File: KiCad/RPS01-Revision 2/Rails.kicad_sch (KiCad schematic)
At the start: 45 parts, among them U11 LM340MPX-5.0/NOPB, U21 LM340MPX-5.0/NOPB

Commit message: updates
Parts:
- C? (x4), C_FF? (x2): value 0.1u DNI -> 0.1u
- C_FF? (x2): value 0.22u DNI -> 0.22u
- C_FF?: value 22u DNI -> 22u
- C_FF?: value 3.65n DNI -> 3.65n
- C_FF?: value 0.47u DNI -> 0.47u
- C_IN? (x2): value 100u DNI -> 100u
- C_OUT? (x2): value 220u DNI -> 220u
- L?: value 53u DNI -> 53u
- L?: value 37u DNI -> 37u
- R? (x2): value 1k DNI -> 1k
- R?: value 8.87k DNI -> 8.87k
- R?: value 3.16k DNI -> 3.16k
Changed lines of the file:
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@@
       (effects (font (size 1.27 1.27)) (justify left))
     )
-    (property "Value" "0.1u DNI" (at 114.3508 271.2212 0)
+    (property "Value" "0.1u" (at 114.3508 271.2212 0)
       (effects (font (size 1.27 1.27)) (justify left))
     )
@@
       (effects (font (size 1.27 1.27)) (justify right))
     )
-    (property "Value" "0.22u DNI" (at 89.963 104.3448 90)
+    (property "Value" "0.22u" (at 89.963 104.3448 90)
       (effects (font (size 1.27 1.27)) (justify right))
     )
@@
   (symbol (lib_id "Device:C_Polarized") (at 341.63 120.396 0) (unit 1)
     (in_bom yes) (on_board yes) (dnp no) (fields_autoplaced)
-    (property "Reference" "C_OUT?" (at 345.44 118.237 0)
-      (effects (font (size 1.27 1.27)) (justify left))
-    )
-    (property "Value" "220u DNI" (at 345.44 120.777 0)
+    (property "Reference" "C_OUT?" (at 345.44 118.872 0)
+      (effects (font (size 1.27 1.27)) (justify left))
+    )
+    (property "Value" "220u" (at 345.44 121.412 0)
       (effects (font (size 1.27 1.27)) (justify left))
     )
@@
   (symbol (lib_id "Device:C_Polarized") (at 513.08 121.92 0) (unit 1)
     (in_bom yes) (on_board yes) (dnp no) (fields_autoplaced)
-    (property "Reference" "C_OUT?" (at 516.89 119.761 0)
-      (effects (font (size 1.27 1.27)) (justify left))
-    )
-    (property "Value" "220u DNI" (at 516.89 122.301 0)
+    (property "Reference" "C_OUT?" (at 516.89 120.396 0)
+      (effects (font (size 1.27 1.27)) (justify left))
+    )
+    (property "Value" "220u" (at 516.89 122.936 0)
       (effects (font (size 1.27 1.27)) (justify left))
     )
@@
       (effects (font (size 1.27 1.27)))
     )
-    (property "Value" "53u DNI" (at 329.1552 108.8207 90)
+    (property "Value" "53u" (at 329.1552 108.8207 90)
       (effects (font (size 1.27 1.27)))
     )
@@
       (effects (font (size 1.27 1.27)) (justify right))
     )
-    (property "Value" "22u DNI" (at 91.44 35.56 90)
+    (property "Value" "22u" (at 91.44 35.56 90)
       (effects (font (size 1.27 1.27)) (justify right))
     )
@@
       (effects (font (size 1.27 1.27)) (justify left))
     )
-    (property "Value" "0.1u DNI" (at 115.57 224.79 0)
+    (property "Value" "0.1u" (at 115.57 224.79 0)
       (effects (font (size 1.27 1.27)) (justify left))
     )
@@
   (symbol (lib_id "Device:C_Small") (at 130.302 210.058 0) (unit 1)
     (in_bom yes) (on_board yes) (dnp no) (fields_autoplaced)
-    (property "Reference" "C?" (at 133.35 208.7943 0)
-      (effects (font (size 1.27 1.27)) (justify left))
-    )
-    (property "Value" "0.1u DNI" (at 133.35 211.3343 0)
+    (property "Reference" "C?" (at 133.35 209.4293 0)
+      (effects (font (size 1.27 1.27)) (justify left))
+    )
+    (property "Value" "0.1u" (at 133.35 211.9693 0)
       (effects (font (size 1.27 1.27)) (justify left))
     )
@@
       (effects (font (size 1.27 1.27)) (justify right))
     )
-    (property "Value" "3.65n DNI" (at 502.92 76.2 90)
+    (property "Value" "3.65n" (at 502.92 76.2 90)
       (effects (font (size 1.27 1.27)) (justify right))
     )
@@
   (symbol (lib_id "Device:C_Small") (at 130.302 255.778 0) (unit 1)
     (in_bom yes) (on_board yes) (dnp no) (fields_autoplaced)
-    (property "Reference" "C?" (at 133.35 254.5143 0)
-      (effects (font (size 1.27 1.27)) (justify left))
-    )
-    (property "Value" "0.1u DNI" (at 133.35 257.0543 0)
+    (property "Reference" "C?" (at 133.35 255.1493 0)
+      (effects (font (size 1.27 1.27)) (justify left))
+    )
+    (property "Value" "0.1u" (at 133.35 257.6893 0)
       (effects (font (size 1.27 1.27)) (justify left))
     )
@@
       (effects (font (size 1.27 1.27)) (justify right))
     )
-    (property "Value" "0.47u DNI" (at 91.1688 53.3982 90)
+    (property "Value" "0.47u" (at 91.1688 53.3982 90)
       (effects (font (size 1.27 1.27)) (justify right))
     )
@@
       (effects (font (size 1.27 1.27)) (justify right))
     )
-    (property "Value" "0.22u DNI" (at 88.2127 136.3649 90)
+    (property "Value" "0.22u" (at 88.2127 136.3649 90)
       (effects (font (size 1.27 1.27)) (justify right))
     )
@@
   (symbol (lib_id "Device:C_Polarized") (at 266.7 118.11 0) (unit 1)
     (in_bom yes) (on_board yes) (dnp no) (fields_autoplaced)
-    (property "Reference" "C_IN?" (at 270.51 115.951 0)
-      (effects (font (size 1.27 1.27)) (justify left))
-    )
-    (property "Value" "100u DNI" (at 270.51 118.491 0)
+    (property "Reference" "C_IN?" (at 270.51 116.586 0)
+      (effects (font (size 1.27 1.27)) (justify left))
+    )
+    (property "Value" "100u" (at 270.51 119.126 0)
       (effects (font (size 1.27 1.27)) (justify left))
     )
@@
       (effects (font (size 1.27 1.27)) (justify right))
     )
-    (property "Value" "1k DNI" (at 307.34 88.9 90)
+    (property "Value" "1k" (at 307.34 88.9 90)
       (effects (font (size 1.27 1.27)) (justify right))
     )
@@
       (effects (font (size 1.27 1.27)) (justify right))
     )
-    (property "Value" "8.87k DNI\n" (at 500.38 90.17 90)
+    (property "Value" "8.87k\n" (at 500.38 90.17 90)
       (effects (font (size 1.27 1.27)) (justify right))
     )
@@
       (effects (font (size 1.27 1.27)) (justify right))
     )
-    (property "Value" "1k DNI" (at 481.33 90.17 90)
+    (property "Value" "1k" (at 481.33 90.17 90)
       (effects (font (size 1.27 1.27)) (justify right))
     )
@@
       (effects (font (size 1.27 1.27)) (justify right))
     )
-    (property "Value" "3.16k DNI" (at 328.93 88.9 90)
+    (property "Value" "3.16k" (at 328.93 88.9 90)
       (effects (font (size 1.27 1.27)) (justify right))
     )
@@
       (effects (font (size 1.27 1.27)) (justify right))
     )
-    (property "Value" "0.1u DNI" (at 130.5444 135.6786 90)
+    (property "Value" "0.1u" (at 130.5444 135.6786 90)
       (effects (font (size 1.27 1.27)) (justify right))
     )
@@
   (symbol (lib_id "Device:C_Polarized") (at 438.15 119.38 0) (unit 1)
     (in_bom yes) (on_board yes) (dnp no) (fields_autoplaced)
-    (property "Reference" "C_IN?" (at 441.96 117.221 0)
-      (effects (font (size 1.27 1.27)) (justify left))
-    )
-    (property "Value" "100u DNI" (at 441.96 119.761 0)
+    (property "Reference" "C_IN?" (at 441.96 117.856 0)
+      (effects (font (size 1.27 1.27)) (justify left))
+    )
+    (property "Value" "100u" (at 441.96 120.396 0)
       (effects (font (size 1.27 1.27)) (justify left))
     )
@@
   (symbol (lib_id "Device:L") (at 500.38 111.76 90) (unit 1)
     (in_bom yes) (on_board yes) (dnp no) (fields_autoplaced)
-    (property "Reference" "L?" (at 500.38 106.68 90)
-      (effects (font (size 1.27 1.27)))
-    )
-    (property "Value" "37u DNI" (at 500.38 109.22 90)
+    (property "Reference" "L?" (at 500.38 107.95 90)
+      (effects (font (size 1.27 1.27)))
+    )
+    (property "Value" "37u" (at 500.38 110.49 90)
       (effects (font (size 1.27 1.27)))
     )
@@
       (effects (font (size 1.27 1.27)) (justify right))
     )
-    (property "Value" "0.1u DNI" (at 131.6717 105.1986 90)
-      (effects (font (size 1.27 1.27)) (justify right))
-    )
+    (property "Value" "0.1u" (at 131.6717 105.1986 90)
+      (effects (font (size 1.27 1.27)) (justify right))
+    )

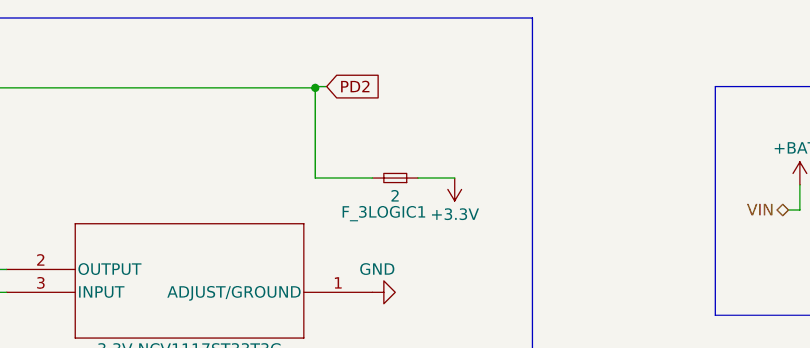
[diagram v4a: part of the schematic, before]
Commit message: Add Jumper for 3.3V Logic
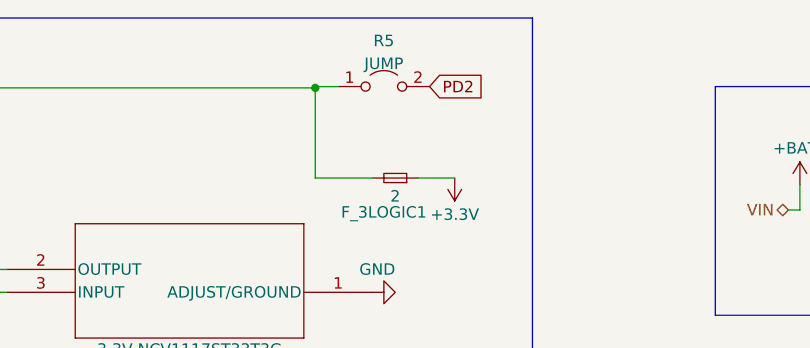
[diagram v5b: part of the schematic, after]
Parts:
- added R5: JUMP, Jumper:SolderJumper-2_P1.3mm_Open_TrianglePad1.0x1.5mm, symbol Jumper:Jumper_2_Open
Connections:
- net PD2: now also R5.2 (B); no longer C_FF?.1, F_3LOGIC1.2
- new net: C_FF?.1, F_3LOGIC1.2, R5.1 (A)
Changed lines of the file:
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@@
+    (stroke (width 0) (type default))
+  )
+  (wire (pts (xy 134.62 26.8134) (xy 134.62 36.83))
     (stroke (width 0) (type default))
   )
@@
     (stroke (width 0) (type default))
   )
+  (wire (pts (xy 134.62 26.67) (xy 137.16 26.67))
+    (stroke (width 0) (type default))
+  )
   (wire (pts (xy 466.09 130.81) (xy 485.14 130.81))
     (stroke (width 0.5) (type default))
@@
     (stroke (width 0) (type default))
   )
-  (wire (pts (xy 135.89 26.67) (xy 134.62 26.67))
-    (stroke (width 0) (type default))
-  )
   (wire (pts (xy 513.08 81.28) (xy 508 81.28))
     (stroke (width 0) (type default))
@@
     (stroke (width 0) (type default))
   )
-  (wire (pts (xy 134.62 26.8134) (xy 134.62 36.83))
-    (stroke (width 0) (type default))
-  )
   (wire (pts (xy 97.79 49.53) (xy 100.33 49.53))
     (stroke (width 0) (type default))
@@
     (stroke (width 0) (type default))
   )
-  (wire (pts (xy 134.62 26.8134) (xy 134.62 26.67))
+  (wire (pts (xy 134.62 26.67) (xy 134.62 26.8134))
     (stroke (width 0) (type default))
   )
@@
     )
   )
-  (global_label "PD2" (shape input) (at 135.89 26.67 0) (fields_autoplaced)
+  (global_label "PD2" (shape input) (at 147.32 26.67 0) (fields_autoplaced)
     (effects (font (size 1.27 1.27)) (justify left))
-    (property "Intersheetrefs" "${INTERSHEET_REFS}" (at 142.5453 26.67 0)
+    (property "Intersheetrefs" "${INTERSHEET_REFS}" (at 153.9753 26.67 0)
       (effects (font (size 1.27 1.27)) (justify left) hide)
     )
@@
         )
       )
+    )
+  )
+  (symbol (lib_id "Jumper:Jumper_2_Open") (at 142.24 26.67 0) (unit 1)
+    (in_bom yes) (on_board yes) (dnp no) (fields_autoplaced)
+    (property "Reference" "R5" (at 142.24 21.59 0)
+      (effects (font (size 1.27 1.27)))
+    )
+    (property "Value" "JUMP" (at 142.24 24.13 0)
+      (effects (font (size 1.27 1.27)))
+    )
+    (property "Footprint" "Jumper:SolderJumper-2_P1.3mm_Open_TrianglePad1.0x1.5mm" (at 142.24 26.67 0)
+      (effects (font (size 1.27 1.27)) hide)
+    )
+    (property "Datasheet" "~" (at 142.24 26.67 0)
+      (effects (font (size 1.27 1.27)) hide)
+    )
+    (pin "1")
+    (pin "2")
+    (instances
+      (project "rps01"
+        (path "/14930f15-c0a0-4b55-93e6-b112548415f6/6ed54b0f-f89c-4a82-b1ab-c92c0c126d05"
+          (reference "R5") (unit 1)
+        )
+      )

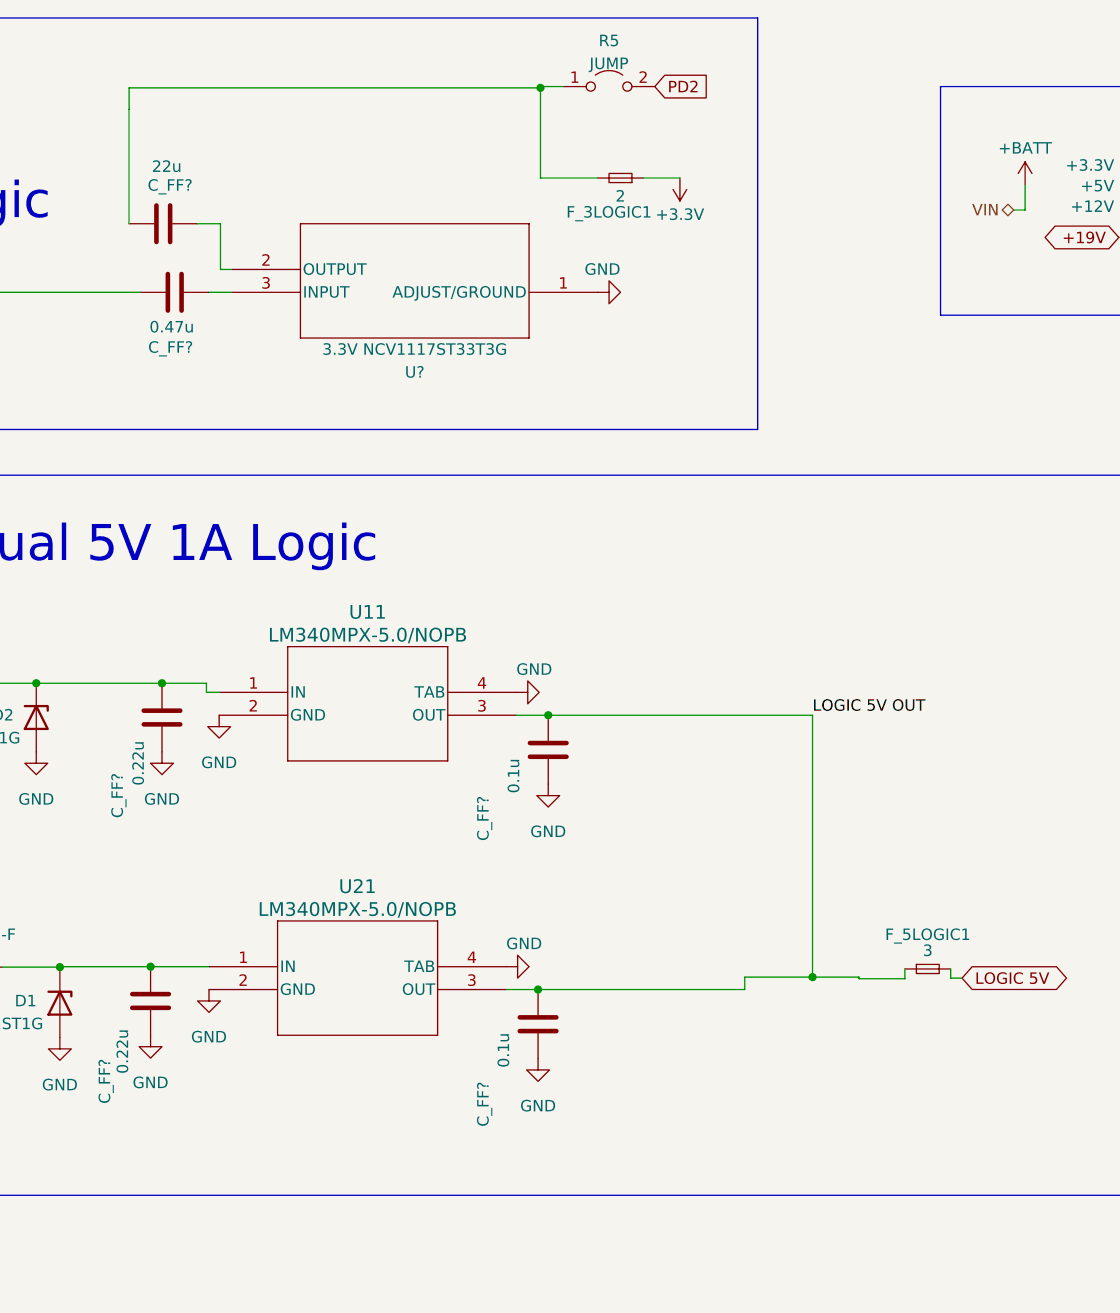
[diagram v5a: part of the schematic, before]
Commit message: Deleted one of the caps
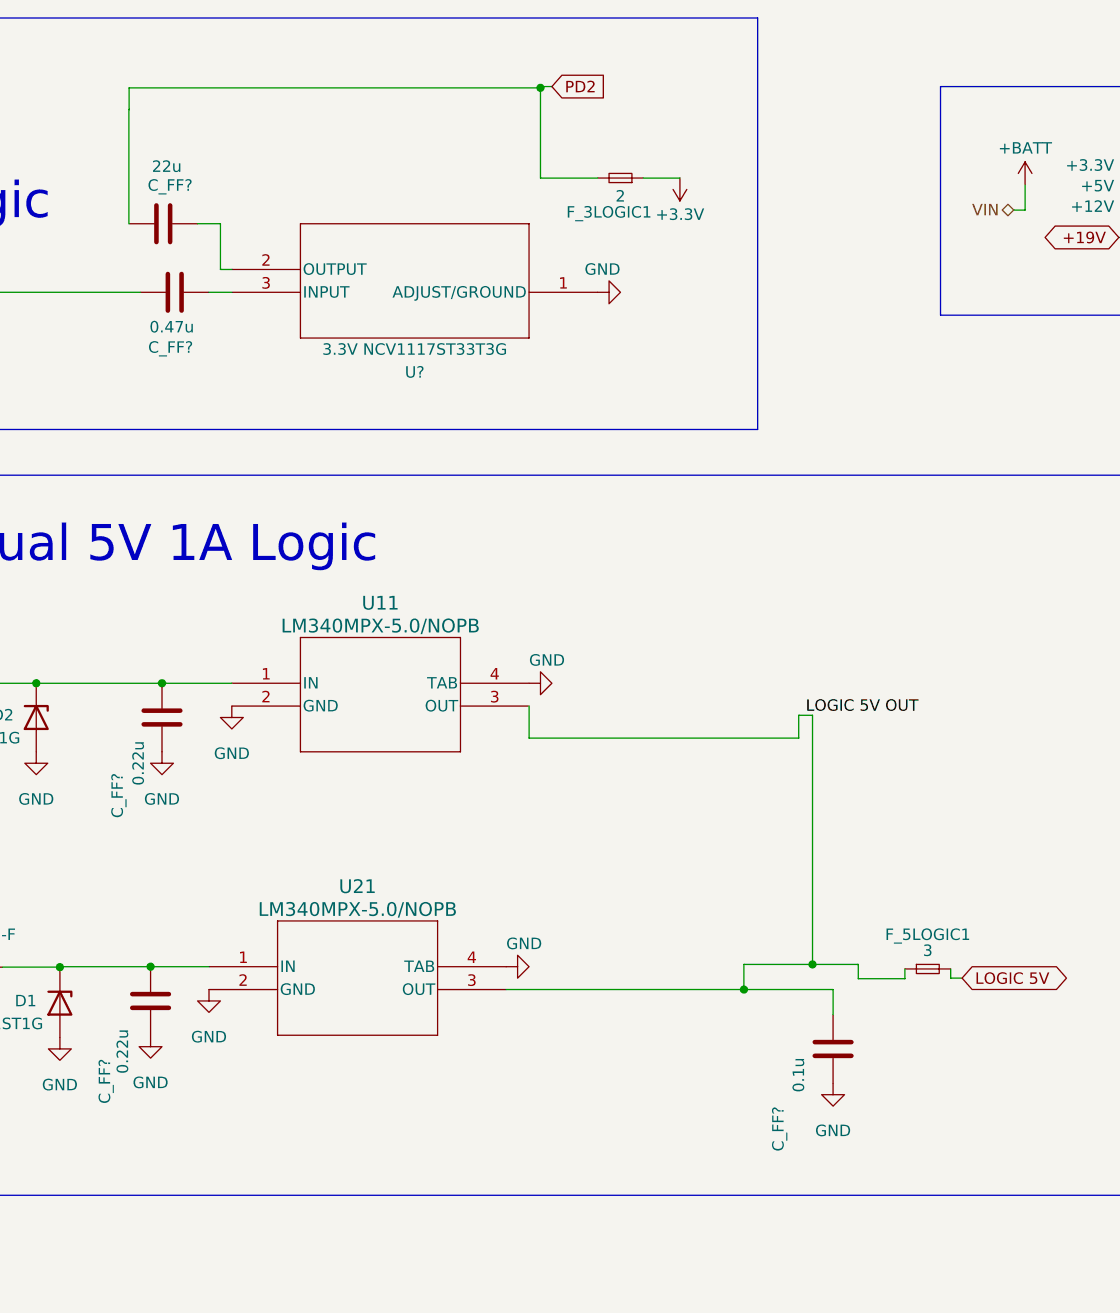
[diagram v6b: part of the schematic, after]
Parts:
- removed C_FF?: 0.1u, Capacitor_SMD:C_0603_1608Metric, symbol Device:C
- removed R5: JUMP, Jumper:SolderJumper-2_P1.3mm_Open_TrianglePad1.0x1.5mm, symbol Jumper:Jumper_2_Open
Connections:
- net PD2: now also C_FF?.1, F_3LOGIC1.2
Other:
- moved on the sheet: C_FF?, U11

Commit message: lOGIC POWER ALMOST DONE
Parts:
- removed C?: 0.1u, Capacitor_SMD:C_0603_1608Metric, symbol Device:C_Small
- removed C_FF?: 0.1u, Capacitor_SMD:C_0603_1608Metric, symbol Device:C
- removed R6: 0, Resistor_SMD:R_0603_1608Metric, symbol Device:R_Small
- R3_12VB1, R3_5VB1: value DNI -> 0 DNI
- R4_12VB1, R4_5VB1: value DNI -> 4.7K DNI
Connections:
- net at C?.1, R6.1, U?.4 (VOUT): now also U?.4 (VOUT)

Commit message: Push before Jason changes 3.3V
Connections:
- net LOGIC5IN2: now reaches C_FF?.2, D1.1 (K), D6.1 (K), U21.1 (IN)
- net LOGIC5IN1: now reaches C_FF?.2, D2.1 (K), D5.1 (K), U11.1 (IN)
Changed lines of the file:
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@@
     (effects (font (size 4 4)) (justify left bottom))
+  )
+  (label "LOGIC5IN1" (at 81.026 92.964 0) (fields_autoplaced)
+    (effects (font (size 1.27 1.27)) (justify left bottom))
+  )
+  (label "LOGIC5IN2" (at 83.058 124.46 0) (fields_autoplaced)
+    (effects (font (size 1.27 1.27)) (justify left bottom))
   )
   (label "LOGIC 5V OUT" (at 164.084 96.52 0) (fields_autoplaced)
